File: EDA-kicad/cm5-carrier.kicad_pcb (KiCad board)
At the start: 6 copper layers, 82 x 155 mm, 133 parts, among them J1 USBC-4-0-CX90MW9-24P1, J2 SIM-G85D1160022HHR, J3 FINGER, J4 SJ2-35894B-SMT-TR, SW1 EG25-switch-CSS-1210MC, SW2 MIC-switch-CSS-1210MC, SW3 CAM-switch-CSS-1210MC, SW4 PROG, SW5 VOL-, SW6 VOL+, SW7 POW, U1 EG25GGC-128-SGNS, U10 22V-boost-AP3032KTR-G1, U11 MP3429GL-Z, U12 FPC15pin-1mm-pitch-F52Q-1A7H1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, U13 Flash-LED-Lumiled, U14 HD3SS460RHRR, U15 USB SWITCH 2CHANNEL TS3USB221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, U4 CODEC-TLV320AIC3204IRHBR, U7 BQ25792RQMR, U9 BAT-CONNECTOR-FLTS22WR00

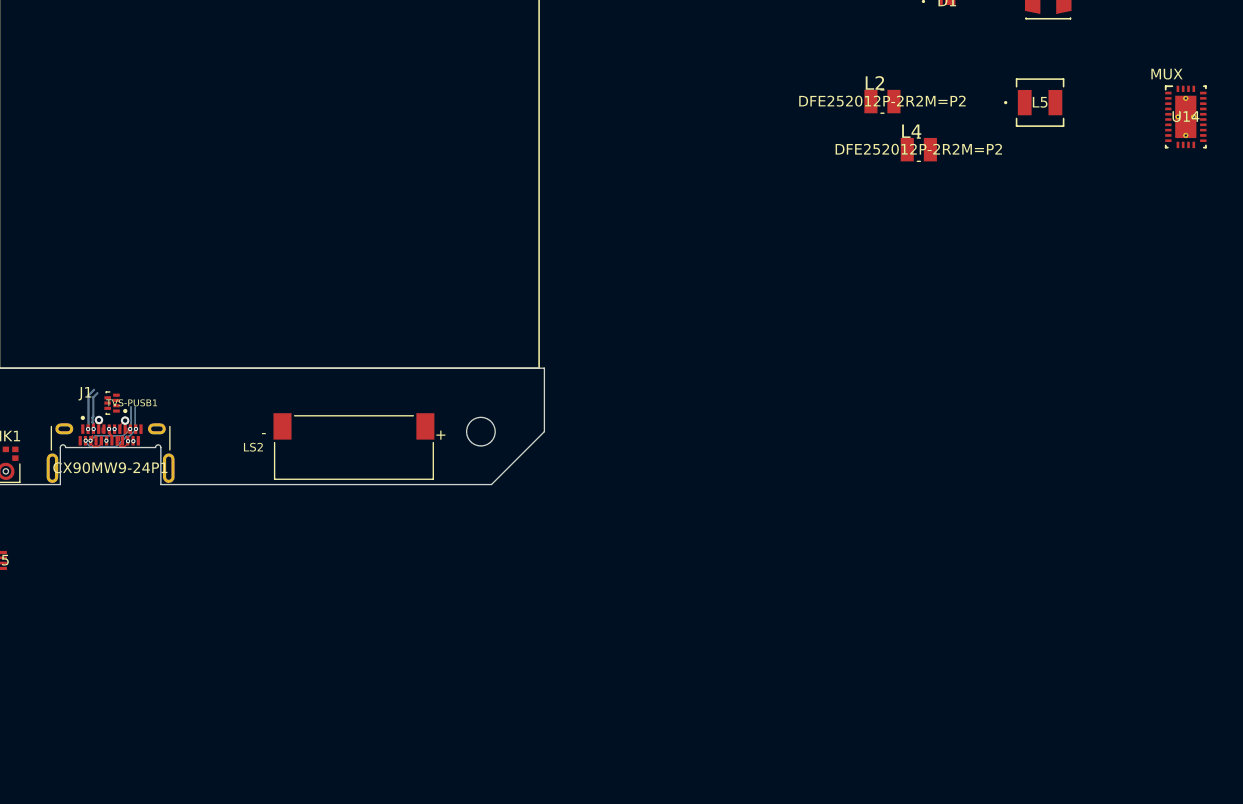
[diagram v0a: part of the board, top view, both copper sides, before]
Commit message: added polarity detection
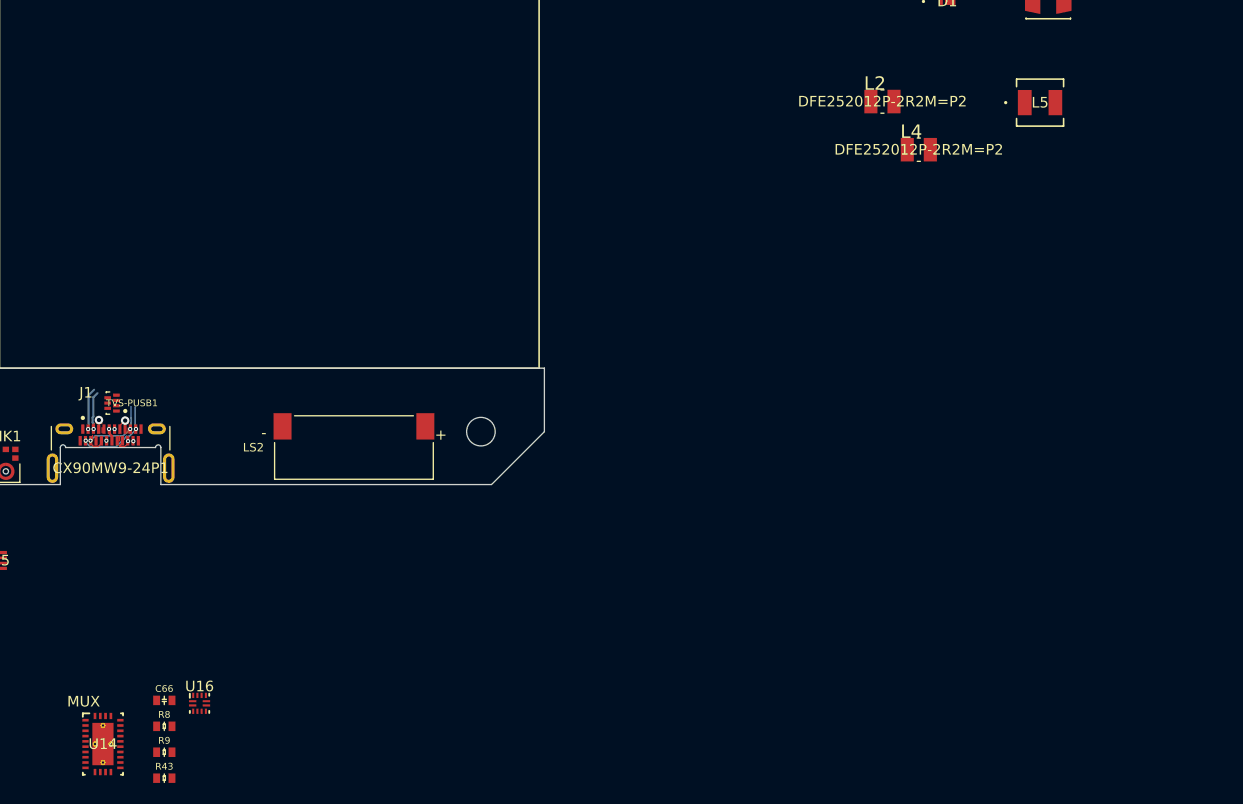
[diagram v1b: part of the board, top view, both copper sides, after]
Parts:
- added C66: 0.1uF, SPIRIT-footprints:0603-capacitor, F.Cu at (100.1, 206.4)
- added R43: 10kΩ, SPIRIT-footprints:0603-resistor, F.Cu at (100.1, 213.8)
- added R8: 10kΩ, SPIRIT-footprints:0603-resistor, F.Cu at (100.1, 208.8)
- added R9: 10kΩ, SPIRIT-footprints:0603-resistor, F.Cu at (100.1, 211.3)
- added U16: usb-polarity-TUSB321RWBR, SPIRIT-footprints:polarity-usb-TUSB321RWBR, F.Cu at (103.4, 206.7)
- U14: value HD3SS460RHRR -> MUX HD3SS460RHRR
- moved U14 118.3 mm to (94.3, 210.5)
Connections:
- net CAM-SWITCH renamed CAM SWITCH
- net EN3V3A-SW-OUT renamed EN3V3A SW OUT
- net ~{LOW_BAT} renamed ~{LOW BAT}
- Module1 pad 163: D+ -> SYS D+
- Module1 pad 165: D- -> SYS D-
- U10 pad 4: LCD_PWM -> LCD PWM
- U14 pad 1: unconnected-(U14-CRX1P-Pad1) -> RX1+
- U14 pad 10: unconnected-(U14-CRX2N-Pad10) -> RX1-
- U14 pad 17: unconnected-(U14-EN-Pad17) -> Net-(U14-EN)
- U14 pad 2: unconnected-(U14-CRX1N-Pad2) -> RX1-
- U14 pad 22: unconnected-(U14-VCC-Pad22) -> 3V3B
- U14 pad 25: unconnected-(U14-SSTXN-Pad25) -> SSTX2+
- U14 pad 26: unconnected-(U14-SSTXP-Pad26) -> SSTX2-
- U14 pad 27: unconnected-(U14-SSRXN-Pad27) -> SSTR2-
- U14 pad 28: unconnected-(U14-SSRXP-Pad28) -> SSTR2+
- U14 pad 29: unconnected-(U14-PAD-Pad29) -> GND
- U14 pad 3: unconnected-(U14-POL-Pad3) -> MUX POL
- U14 pad 4: unconnected-(U14-CTX1P-Pad4) -> TX1+
- U14 pad 5: unconnected-(U14-CTX1N-Pad5) -> TX1-
- U14 pad 6: unconnected-(U14-CTX2P-Pad6) -> TX1+
- U14 pad 7: unconnected-(U14-CTX2N-Pad7) -> TX1-
- U14 pad 8: unconnected-(U14-AMSEL-Pad8) -> Net-(U14-AMSEL)
- U14 pad 9: unconnected-(U14-CRX2P-Pad9) -> RX1+
- U15 pad 1: unconnected-(U15-1D+-Pad1) -> SYS D+
- U15 pad 10: unconnected-(U15-VCC-Pad10) -> 3V3B
- U15 pad 2: unconnected-(U15-1D--Pad2) -> SYS D-
- U15 pad 3: unconnected-(U15-2D+-Pad3) -> CHARGER D+
- U15 pad 4: unconnected-(U15-2D--Pad4) -> CHARGER D-
- U15 pad 5: unconnected-(U15-GND-Pad5) -> GND
- U15 pad 6: unconnected-(U15-*OE-Pad6) -> GND
- U15 pad 7: unconnected-(U15-D--Pad7) -> D-
- U15 pad 8: unconnected-(U15-D+-Pad8) -> D+
- U15 pad 9: unconnected-(U15-S-Pad9) -> USB SWITCH
- U7 pad 6: D+ -> CHARGER D+
- U7 pad 7: D- -> CHARGER D-
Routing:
- net D+: track 2.20 -> 1.20 mm
- net CHARGER D+: track 0.00 -> 0.99 mm
- net D-: track 2.34 -> 1.41 mm
- net CHARGER D-: track 0.00 -> 0.93 mm
